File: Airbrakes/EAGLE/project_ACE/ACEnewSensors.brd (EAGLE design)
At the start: 100.3 x 62.2 mm, 21 parts, among them J3 PTH

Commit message: Finalize v0.2 ACE PCB
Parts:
- removed R1: 0 ohm, fab_new:R1206
- removed R2, R3: (no value), fab_new:R1206
- added JP4, JP5: STAND-OFF, SparkFun:STAND-OFF
- moved SERVO 8.27 mm to (112.6, 49.9)
- moved U$14 2.58 mm to (118.5, 63.0)
- moved U$13 2.44 mm to (26.5, 63.0)
- moved 7.4POWER 2.07 mm to (101.0, 61.2)
- moved ROTARY_TERMINAL 2.07 mm to (89.7, 61.2)
- moved U$5 2.07 mm to (29.3, 41.0)
- moved JP2 2.07 mm to (37.8, 19.4)
- moved JP3 2.07 mm to (37.8, 32.1)
- moved U$10 2.07 mm to (88.6, 22.0)
- moved U$8 1.82 mm to (68.6, 41.8)
- moved U$9 1.82 mm to (66.1, 41.8)
- moved J3 1.82 mm to (66.1, 40.1)
- moved U$16 1.82 mm to (71.2, 41.9)
- moved U$19 1.82 mm to (73.7, 41.9)
- moved U$15 1.77 mm to (26.6, 9.03)
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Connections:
- removed net 3.3V: J3.2, JP1.2, U$10.J17
- removed net VIN: JP1.1
- net GND: no longer R1.1
- net N$2: now also JP1.2; no longer R2.2, R3.1
- net SDA: no longer R2.1, R3.2
- net SERVO_PWM: now also U$10.J25; no longer U$10.J9
- net VCC: now also J3.2, JP1.1, U$10.J17; no longer U$10.J15
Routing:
- net GND: track 205.1 -> 0.00 mm
- net VCC: track 112.4 -> 0.00 mm
- net 3.3V: track 73.6 -> 0.00 mm
- net SCL: track 150.1 -> 205.1 mm
- net SDA: track 122.5 -> 162.0 mm
- net SERVO_PWM: track 51.0 -> 70.1 mm
- net N$2: track 17.7 -> 0.00 mm
- net SERVO_VIN: track 8.89 -> 12.4 mm
- added copper zone on layer 1, net VCC
- removed copper zone on layer 1, net GND
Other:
- board size 100.3 x 62.2 mm -> 100 x 63 mm
- board text added: "A C E"
- board text added: "AIRBRAKES COMPUTE ELEMENT"
- board text added: "May all who install this ACE onto a subscale or fullscale vehicle become the recipients of great fortune and success..."
- board text added: "v0.2 (...no more on-field soldering!)"

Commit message: Added MPM3630
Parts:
- added U1: MPM3630GQV-P, MPM3630:QFN3P0X5P0X1P6_MPM3630_MNP
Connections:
- new net N$3: U1.17
- new net N$4: U$10.J16, U1.9
- new net N$5: U1.2
- new net N$6: U1.18
- new net N$7: U1.1
- net GND: now also U1.14, U1.3
- net SERVO_VIN: now also U1.16
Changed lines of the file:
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@@
 <element name="JP4" library="SparkFun" package="STAND-OFF" value="STAND-OFF" x="59.69" y="62.992" smashed="yes"/>
 <element name="JP5" library="SparkFun" package="STAND-OFF" value="STAND-OFF" x="80.01" y="62.992" smashed="yes"/>
+<element name="U1" library="MPM3630" package="QFN3P0X5P0X1P6_MPM3630_MNP" value="MPM3630GQV-P" x="110" y="38.5" smashed="yes">
+<attribute name="COPYRIGHT" value="Copyright (C) 2024 Ultra Librarian. All rights reserved." x="110" y="38.5" size="1.778" layer="27" display="off"/>
+<attribute name="MANUFACTURER_PART_NUMBER" value="MPM3630GQV-P" x="110" y="38.5" size="1.778" layer="27" display="off"/>
+<attribute name="MFR_NAME" value="Monolithic Power Systems" x="110" y="38.5" size="1.778" layer="27" display="off"/>
+<attribute name="NAME" x="106.7234" y="37.865" size="1.27" layer="27" ratio="6" rot="SR0"/>
+<attribute name="VALUE" x="108.2728" y="37.865" size="1.27" layer="27" ratio="6" rot="SR0"/>
+</element>
 </elements>
 <signals>
@@
 <vertex x="22.5" y="4.5"/>
 </polygon>
+<contactref element="U1" pad="3"/>
+<contactref element="U1" pad="14"/>
+<wire x1="91.948" y1="41.37" x2="113.284" y2="49.911" width="0" layer="19" extent="1-1"/>
+<wire x1="87.122" y1="61.214" x2="91.948" y2="41.37" width="0" layer="19" extent="1-1"/>
+<wire x1="66.092" y1="40.145" x2="91.948" y2="41.37" width="0" layer="19" extent="1-1"/>
+<wire x1="42.01" y1="44.844" x2="66.092" y2="40.145" width="0" layer="19" extent="1-1"/>
+<wire x1="34.036" y1="32.131" x2="42.01" y2="44.844" width="0" layer="19" extent="1-1"/>
+<wire x1="36.576" y1="19.431" x2="34.036" y2="32.131" width="0" layer="19" extent="1-1"/>
+<wire x1="110.75" y1="40.944" x2="36.576" y2="19.431" width="0" layer="19" extent="1-1"/>
+<wire x1="108.746" y1="38.75" x2="110.75" y2="40.944" width="0" layer="19" extent="1-1"/>
+<wire x1="91.9304" y1="11.8494" x2="91.948" y2="41.37" width="0" layer="19" extent="1-1"/>
 </signal>
 <signal name="VCC" class="2">
@@
 <contactref element="U$10" pad="J17"/>
 <contactref element="J3" pad="2"/>
+<wire x1="68.632" y1="40.145" x2="86.868" y2="41.37" width="0" layer="19" extent="1-1"/>
+<wire x1="94.4704" y1="11.8494" x2="86.868" y2="41.37" width="0" layer="19" extent="1-1"/>
+<wire x1="36.93" y1="44.844" x2="68.632" y2="40.145" width="0" layer="19" extent="1-1"/>
+<wire x1="31.496" y1="19.431" x2="36.93" y2="44.844" width="0" layer="19" extent="1-1"/>
 </signal>
 <signal name="SCL">
@@
 <wire x1="113.284" y1="54.991" x2="109.728" y2="54.991" width="1.016" layer="1"/>
 <wire x1="103.505" y1="61.214" x2="109.728" y2="54.991" width="1.016" layer="1"/>
+<contactref element="U1" pad="16"/>
+<wire x1="109.75" y1="40.754" x2="103.505" y2="61.214" width="0" layer="19" extent="1-1"/>
 </signal>
 <signal name="SERVO_GND">
@@
 <contactref element="JP1" pad="2"/>
 </signal>
+<signal name="N$5">
+<contactref element="U1" pad="2"/>
+</signal>
+<signal name="N$6">
+<contactref element="U1" pad="18"/>
+</signal>
+<signal name="N$3">
+<contactref element="U1" pad="17"/>
+</signal>
+<signal name="N$4">
+<contactref element="U1" pad="9"/>
+<contactref element="U$10" pad="J16"/>
+<wire x1="111.546" y1="38.1" x2="97.0104" y2="11.8494" width="0" layer="19" extent="1-1"/>
+</signal>
+<signal name="N$7">
+<contactref element="U1" pad="1"/>
+</signal>
 </signals>

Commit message: PACE Start
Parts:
- removed SERVO: (no value), con-wago-508:W237-3E
- added C1, C2, C2A: CL31B226KPHNNNE, 22uF_Capacitor:CAP_CL31_SAM
- added C4: 885012005009, 22pF_Capacitor:CAP_885012005_WRE
- added J1, J2: 10118192-0002LF, USB_Micro_B:CONN_10118192-0002LF_AMP
- added R1: ERJ-3EKF5102V, 51kO_Resistor:RC0603N_PAN
- added R2: ERA3AEB6981V, 6_98kO_Resistor:RES_ERA3A_0603_PAN
- added R3: RM04F1003CT, 100kO_Resistor:RES_RM04_CCE
- added R5: RC1005F103CS, 10kO_Resistor:RES_1005_SAM
- added SERVOCON: B03B-PASK-1_(LF)_(SN), 3_Pin_JST_XA_Surface_Connector:CONN_B03B-PASK-1_(LF)_(SN)_JST
- moved U1 92.5 mm to (18.0, 48.0)
- moved 7.4POWER 68.0 mm to (33.0, 61.7)
- moved ROTARY_TERMINAL 67.5 mm to (22.2, 61.7)
- moved U$15 15.0 mm to (11.6, 8.03)
- moved U$13 14.5 mm to (12.0, 63.5)
- moved JP1 9.92 mm to (103.3, 47.9)
- moved U$1 9.92 mm to (95.0, 59.3)
- moved U$3 9.92 mm to (111.5, 59.3)
- moved J3 8.02 mm to (74.1, 40.6)
- moved JP4 8.02 mm to (67.7, 63.5)
- moved JP5 8.02 mm to (88.0, 63.5)
- moved U$16 8.02 mm to (79.2, 42.4)
- moved U$19 8.02 mm to (81.7, 42.4)
- moved U$8 8.02 mm to (76.6, 42.3)
- moved U$9 8.02 mm to (74.1, 42.3)
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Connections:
- removed net N$6: U1.18
- new net PWR_GD: R5.2, U1.18
- net GND: now also C1.1, C2.2, C2A.2, J1.5, J2.5, R2.1, SERVOCON.2; no longer SERVO.2
- net N$3: now also R3.1
- net N$4: now also C2.1, C2A.1, C4.2, J1.1, J2.1, R1.1, U1.7, U1.8
- net N$5: now also R5.1
- net N$7: now also C4.1, R1.2, R2.2
- net SERVO_PWM: now also SERVOCON.3; no longer SERVO.1
- net SERVO_VIN: now also C1.2, R3.2, SERVOCON.1; no longer SERVO.3
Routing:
- net GND: track 0.00 -> 263.9 mm, vias 0 -> 5
- net VCC: track 0.00 -> 141.6 mm, vias 0 -> 2
- net N$4: track 0.00 -> 131.8 mm, vias 0 -> 2
- net SERVO_VIN: track 12.4 -> 126.1 mm
- net SCL: track 205.1 -> 160.6 mm
- net SDA: track 162.0 -> 146.0 mm
- net SERVO_PWM: track 70.1 -> 65.5 mm
- net N$5: track 0.00 -> 4.33 mm, vias 0 -> 2
- net N$7: track 0.00 -> 2.81 mm
- net PWR_GD: track 0.00 -> 2.27 mm
- net N$3: track 0.00 -> 1.19 mm
- net SERVO_GND: track 6.22 -> 5.72 mm
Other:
- board size 100 x 63 mm -> 114.5 x 63 mm
- board text added: "P A C E"
- board text added: "POWER & AIRBRAKES COMPUTE ELEMENT"
- board text removed: "+"
- board text removed: "-"
- board text removed: "7.4v"
- board text removed: "A C E"
- board text removed: "AIRBRAKES COMPUTE ELEMENT"
- board text removed: "GND"
- board text removed: "PWM"
- board text removed: "VIN"

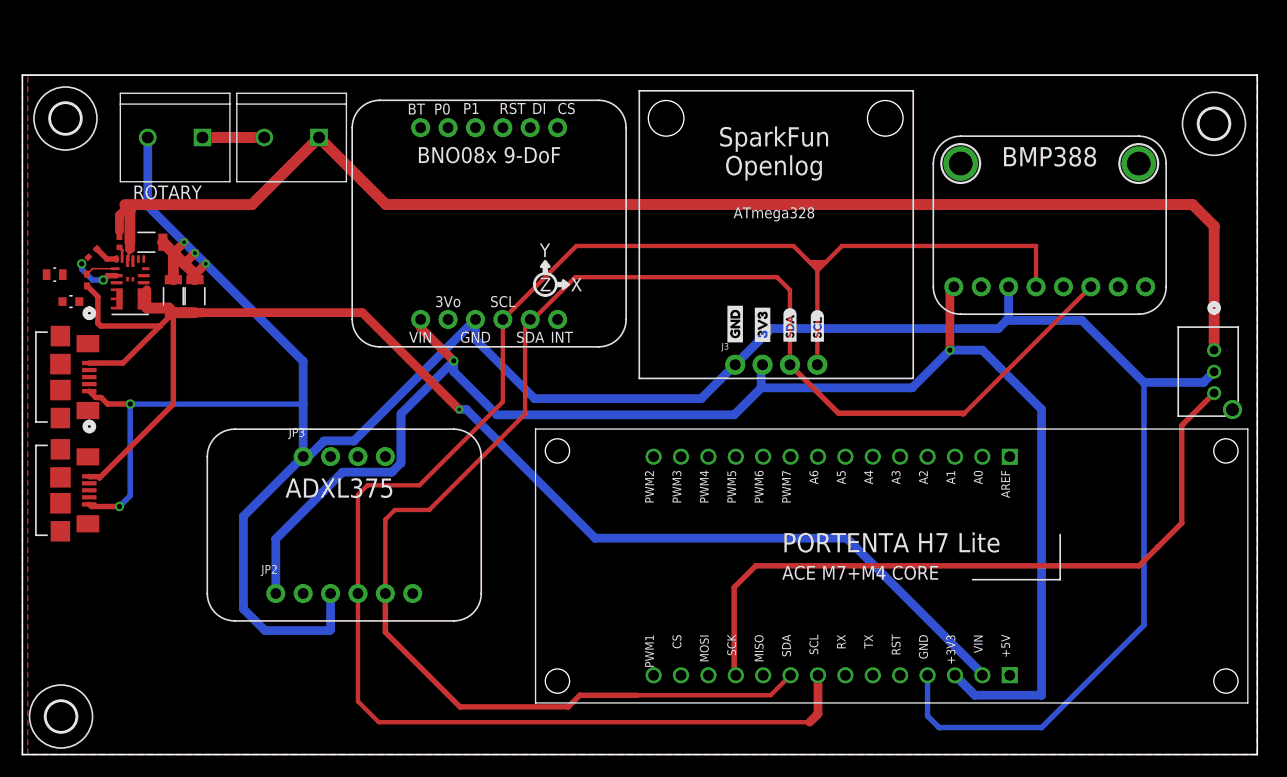
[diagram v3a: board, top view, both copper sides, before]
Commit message: First PACE layout draft (#98)
* WIP refactoring

* First draft of PACE

* Add MPM3630 block

* Finalize PACE board

* Add 51 Ohm resistor part

* Final revisions

---------

Co-authored-by: Breadn <bylueang@gmail.com>
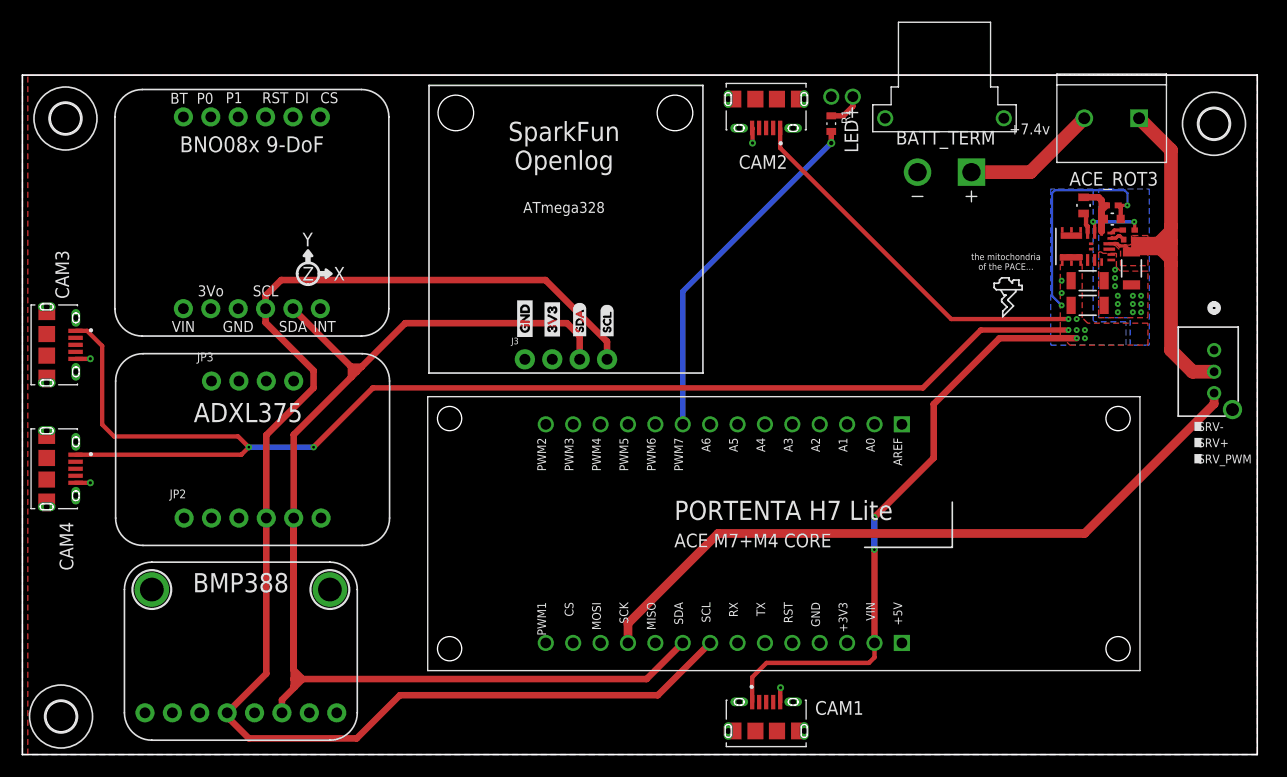
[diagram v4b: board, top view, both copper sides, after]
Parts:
- removed 7.4POWER, ROTARY_TERMINAL: 282837-2, 282837-2:TE_282837-2
- removed C1, C2, C2A: CL31B226KPHNNNE, 22uF_Capacitor:CAP_CL31_SAM
- removed J1, J2: 10118192-0002LF, USB_Micro_B:CONN_10118192-0002LF_AMP
- removed R2: ERA3AEB6981V, 6_98kO_Resistor:RES_ERA3A_0603_PAN
- removed R5: RC1005F103CS, 10kO_Resistor:RES_1005_SAM
- removed U1: MPM3630GQV-P, MPM3630:QFN3P0X5P0X1P6_MPM3630_MNP
- added ACE_ROT3: 282837-2, 282837-2:TE_282837-2
- added BATT_TERM: XT30PW-F, XT30PW-F:AMASS_XT30PW-F
- added C2A1, C5: CL31B226KPHNNNE, 22uF_Capacitor:CAP_CL31_SAM
- added C6: 885012005009, 22pF_Capacitor:CAP_885012005_WRE
- added CAM1, CAM2, CAM3, CAM4: 10118194-0001LF, USB_Micro_B_v2:AMPHENOL_10118194-0001LF
- added R6: RM04F1003CT, 100kO_Resistor:RES_RM04_CCE
- added R7: ERA3AEB6981V, 6_98kO_Resistor:RES_ERA3A_0603_PAN
- added R8: ERJ-3EKF5102V, 51kO_Resistor:RC0603N_PAN
- added U2: MPM3630GQV-P, MPM3630:QFN3P0X5P0X1P6_MPM3630_MNP
- C4: value 885012005009 -> CL31B226KPHNNNE; device 22pF_Capacitor:CAP_885012005_WRE -> 22uF_Capacitor:CAP_CL31_SAM
- R1: value ERJ-3EKF5102V -> ERJ3EKF51R0V; device 51kO_Resistor:RC0603N_PAN -> ERJ3EKF51R0V-51Ohm-Resistor:RES_ERJ3EKF51R0V
- R3: value RM04F1003CT -> RC1005F103CS; device 100kO_Resistor:RES_RM04_CCE -> 10kO_Resistor:RES_1005_SAM
- moved R3 93.6 mm to (110.6, 53.1), turned to 0 degrees
- moved C4 92.8 mm to (106.8, 48.4), turned to 180 degrees
- moved JP1 84.8 mm to (28.3, 8.37)
- moved U$1 84.8 mm to (20.0, 19.8)
- moved U$3 84.8 mm to (36.5, 19.8)
- moved R1 72.4 mm to (83.0, 63.0), turned to 270 degrees
- moved U$5 22.0 mm to (15.3, 42.0)
- moved U$8 19.5 mm to (57.1, 42.8)
- moved J3 19.5 mm to (54.6, 41.1)
- moved JP4 19.5 mm to (48.2, 64.0)
- moved JP5 19.5 mm to (68.5, 64.0)
- moved U$16 19.5 mm to (59.7, 42.9)
- moved U$19 19.5 mm to (62.2, 42.9)
- moved U$9 19.5 mm to (54.6, 42.8)
- moved JP2 11.0 mm to (29.3, 26.4)
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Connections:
- net SERVO_PWM renamed SRV_PWM
- removed net N$3: R3.1, U1.17
- removed net N$4: C2.1, C2A.1, C4.2, J1.1, J2.1, R1.1, U$10.J16, U1.7, U1.8, U1.9
- removed net N$5: R5.1, U1.2
- removed net N$7: C4.1, R1.2, R2.2, U1.1
- removed net PWR_GD: R5.2, U1.18
- removed net SERVO_GND: 7.4POWER.2, ROTARY_TERMINAL.1
- removed net SERVO_VIN: 7.4POWER.1, C1.2, R3.2, SERVOCON.1, U1.16
- new net 5VO: C2A1.2, C4.2, C6.2, CAM1.1, CAM2.1, CAM3.1, CAM4.1, R8.2, U$10.J16, U2.7, U2.8, U2.9
- new net 7.4VCC: ACE_ROT3.1, C5.1, R6.2, SERVOCON.2, U2.16
- new net 7.4VIN: ACE_ROT3.2, BATT_TERM.P
- new net AGND: R7.1, U2.3
- new net EN: R6.1, U2.17
- new net FB: C6.1, R7.2, R8.1, U2.1
- new net LED: R1.2, U$10.J9
- new net MPM_VCC: R3.2, U2.2
- new net PG: R3.1, U2.18
- new net STAT_LED: R1.1
- net GND: now also BATT_TERM.N, C2A1.1, C4.1, C5.2, CAM1.5, CAM2.5, CAM3.5, CAM4.5, SERVOCON.1, U2.12, U2.13, U2.14; no longer C1.1, C2.2, C2A.2, J1.5, J2.5, R2.1, ROTARY_TERMINAL.2, SERVOCON.2, U1.14, U1.3
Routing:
- net GND: track 263.9 -> 5.51 mm, vias 5 -> 17
- net 5VO: track 0.00 -> 234.1 mm, vias 0 -> 15
- net VCC: track 141.6 -> 0.00 mm, vias 2 -> 0
- net N$4: track 131.8 -> 0.00 mm, vias 2 -> 0
- net SERVO_VIN: track 126.1 -> 0.00 mm
- net 7.4VCC: track 0.00 -> 51.7 mm
- net LED: track 0.00 -> 32.9 mm, vias 0 -> 1
- net SCL: track 160.6 -> 129.8 mm
- net SDA: track 146.0 -> 123.9 mm
- net 7.4VIN: track 0.00 -> 12.5 mm
- net FB: track 0.00 -> 8.51 mm
- net SERVO_GND: track 5.72 -> 0.00 mm
- net MPM_VCC: track 0.00 -> 5.68 mm, vias 0 -> 2
- net N$5: track 4.33 -> 0.00 mm, vias 2 -> 0
- net STAT_LED: track 0.00 -> 3.26 mm, vias 0 -> 1
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- added copper zone on layer 1, net 5VO
- added copper zone on layer 16, net 5VO
- added copper zone on layer 1, net 7.4VCC
- added copper zone on layer 1, net GND
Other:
- board text added: "+7.4v"
- board text added: "."
- board text added: "@WURocketry - Airbrakes 2023-2024"
- board text added: "Best of luck and godspeed on your travels..."
- board text added: "LED+"
- board text added: "SRV+"
- board text added: "SRV-"
- board text added: "SRV_PWM"
- board text added: "the mitochondria of the PACE..."
- board text added: "v1.0 (now with more ports!)"
- board text removed: "@WURocketry - Airbrakes 2023"
- board text removed: "May all who install this ACE onto a subscale or fullscale vehicle become the recipients of great fortune and success..."
- board text removed: "ROTARY"
- board text removed: "v0.2 (...no more on-field soldering!)"
